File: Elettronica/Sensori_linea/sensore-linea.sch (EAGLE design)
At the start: 21 parts, among them T1 BP103, T2 BP103, T3 BP103

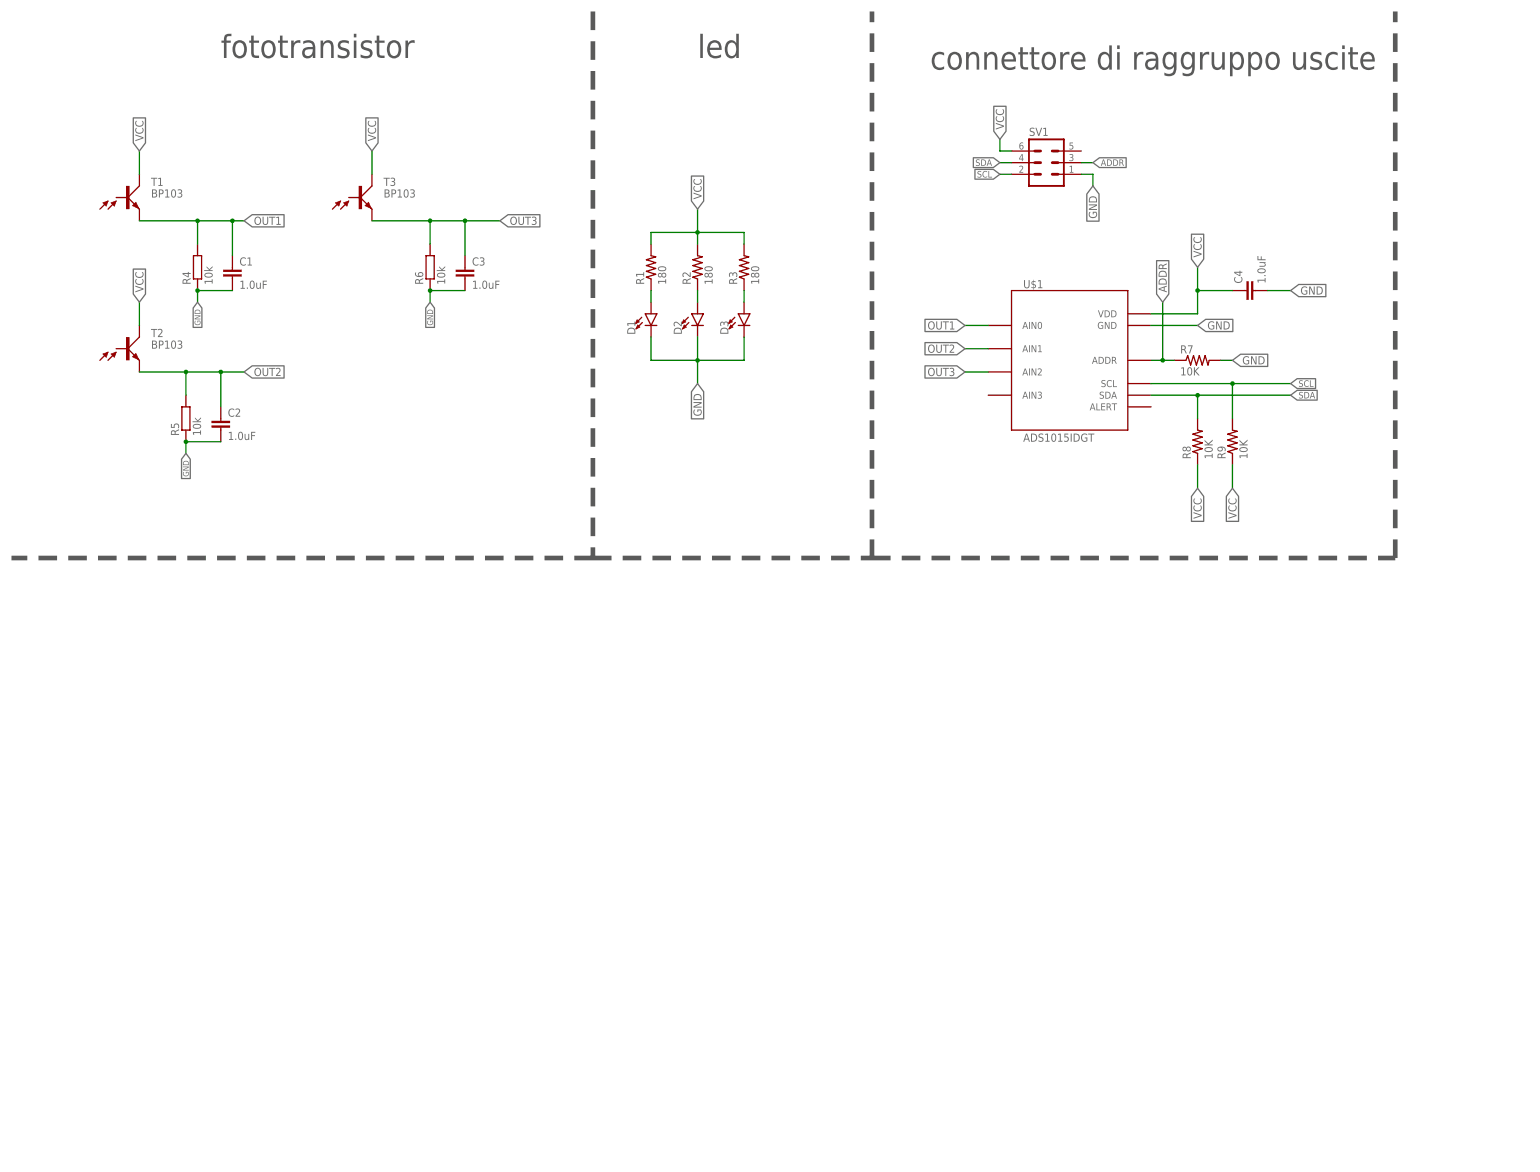
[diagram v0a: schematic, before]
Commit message: Sens linea schematico
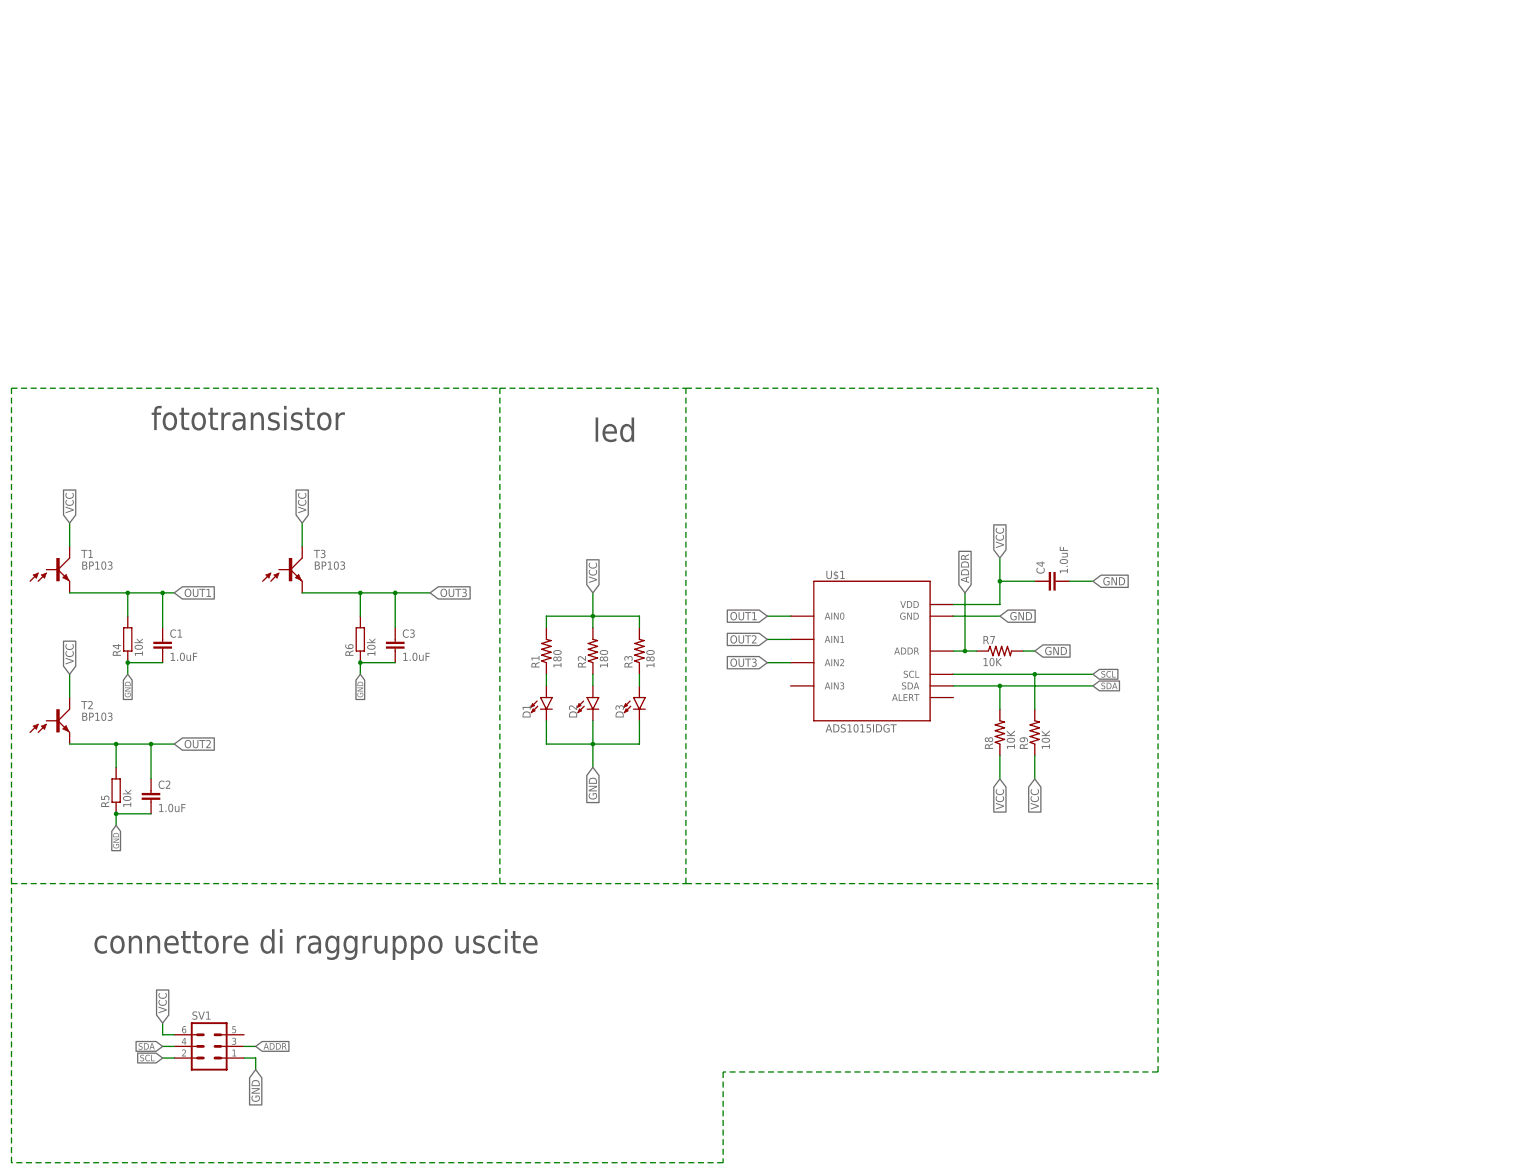
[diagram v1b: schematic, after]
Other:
- moved on the sheet: C1, C2, C3, C4, D1, D2, D3, R1, R2, R3, R4, R5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
